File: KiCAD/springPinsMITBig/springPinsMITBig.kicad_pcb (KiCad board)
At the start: 2 copper layers, 25.1 x 25.1 mm, 21 parts, among them J1 CONN_02X06, J2 CONN_02X06

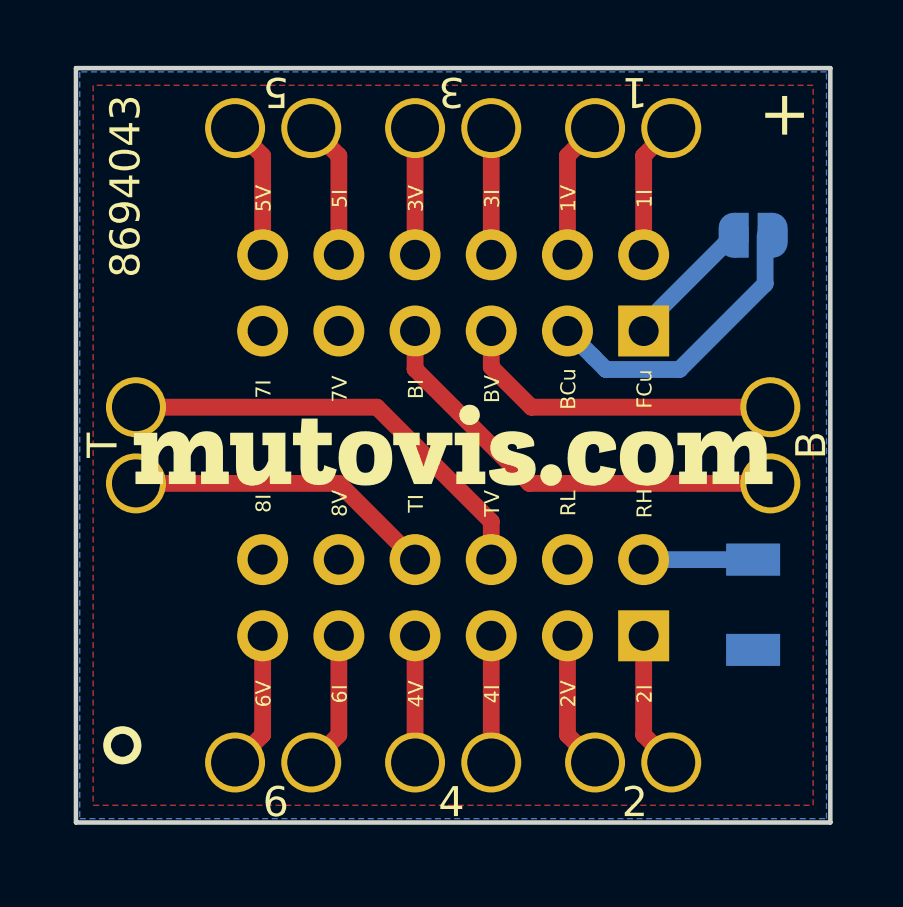
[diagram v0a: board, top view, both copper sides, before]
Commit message: clean up mit springpin board names
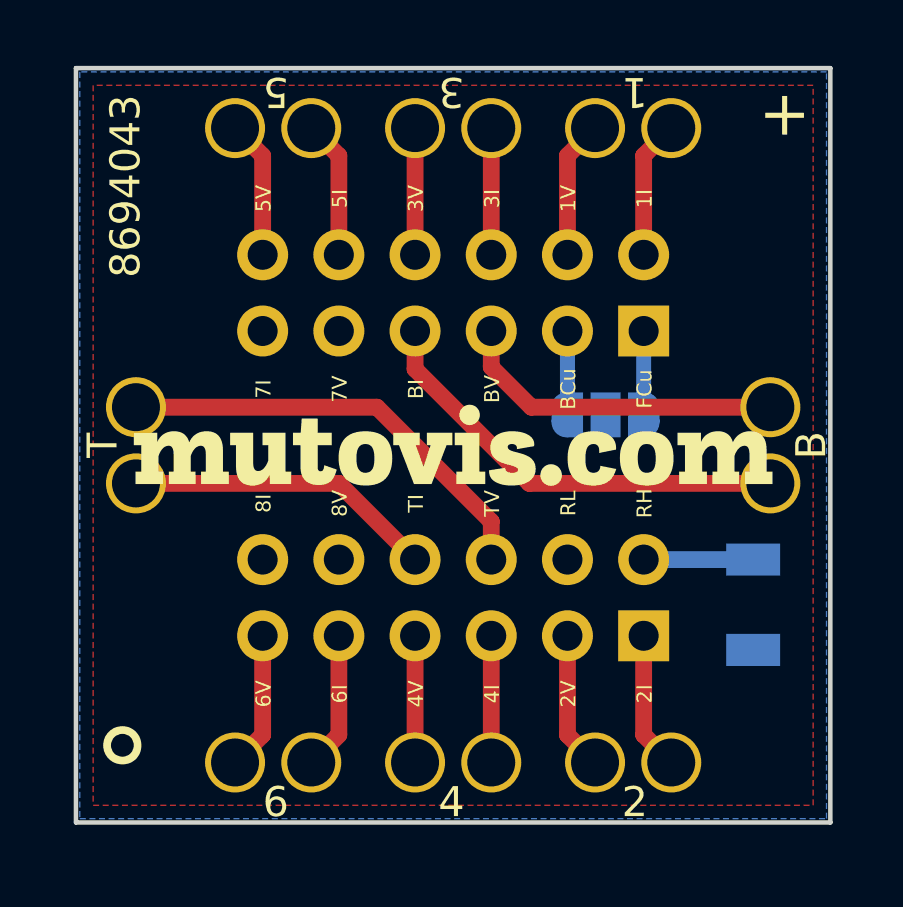
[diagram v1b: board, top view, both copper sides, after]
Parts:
- added L1: grey@mutovis.com, logo:text, B.Cu at (0.00, 0.00)
- JP1: value Jumper_NO_Small -> Jumper_3_Open; footprint Jumper:SolderJumper-2_P1.3mm_Open_RoundedPad1.0x1.5mm -> Jumper:SolderJumper-3_P1.3mm_Open_RoundedPad1.0x1.5mm_NumberLabels
- moved JP1 7.75 mm to (5.08, -1.02), turned to 0 degrees
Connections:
- J2 pad 3: GND -> /BCu
- JP1 pad 1: GND -> /BCu
- JP1 pad 2: /FCu -> GND
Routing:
- net GND: track 9.92 -> 0.00 mm
- net /BCu: track 0.00 -> 2.81 mm
- net /FCu: track 4.43 -> 3.00 mm

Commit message: update holder for mit
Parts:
- J1, J2: footprint Connector_PinHeader_2.54mm:PinHeader_2x06_P2.54mm_Vertical -> myParts:TE_5-103168-4

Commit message: update connector components and design printed bottom header shroud
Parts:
- J1: footprint myParts:TE_5-103168-4 -> myParts:TSSH-106-01-T-D-04
- J2: footprint myParts:TE_5-103168-4 -> myParts:TSSH-106-01-T-D
- moved JP1 7.01 mm to (10.8, -5.08), turned to 270 degrees
- moved R1 1.43 mm to (11.4, 5.32), turned to 270 degrees
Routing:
- net /BCu: track 2.81 -> 14.3 mm
- net GND: track 0.00 -> 10.6 mm
- net /RH: track 3.65 -> 6.33 mm
- net /FCu: track 3.00 -> 4.05 mm
- added copper zone on B.Cu, net /BCu
- removed copper zone on B.Cu, net GND
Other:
- board text added: "NC"
- board text added: "RS"
- board text removed: "RH"
- board text removed: "RL"
